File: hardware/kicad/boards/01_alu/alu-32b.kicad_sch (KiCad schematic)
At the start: 97 parts, among them J1 Conn_02x06_Odd_Even, J2 Conn_02x04_Odd_Even, J3 Conn_02x16_Counter_Clockwise, J4 Conn_02x16_Counter_Clockwise, J5 Conn_02x16_Counter_Clockwise, J6 Conn_02x16_Counter_Clockwise, SW1 SW_DIP_x08, SW10 SW_DIP_x08, SW11 SW_DIP_x08, SW12 SW_DIP_x08, SW13 SW_SPDT, SW2 SW_DIP_x08, SW3 SW_DIP_x08, SW4 SW_DIP_x08, SW5 SW_DIP_x08, SW6 SW_DIP_x08, SW7 SW_DIP_x08, SW8 SW_DIP_x08, SW9 SW_DIP_x08, U1 74HC86, U10 74LS30, U11 74LS182, U12 74LS182, U13 74LS182, U14 74LS30, U15 74LS182, U16 74LS182, U17 74LS182, U18 74LS182, U19 74LS182, U2 74LS153, U20 74LS182, U21 74LS182, U22 74LS182, U23 74LS540, U24 74LS377, U25 74LS377, U3 74AHC541, U4 74HCT00, U5 74AHCT1G08, U6 74AHC1G04, U7 74LS30, U8 74AHC541, U9 74LS30

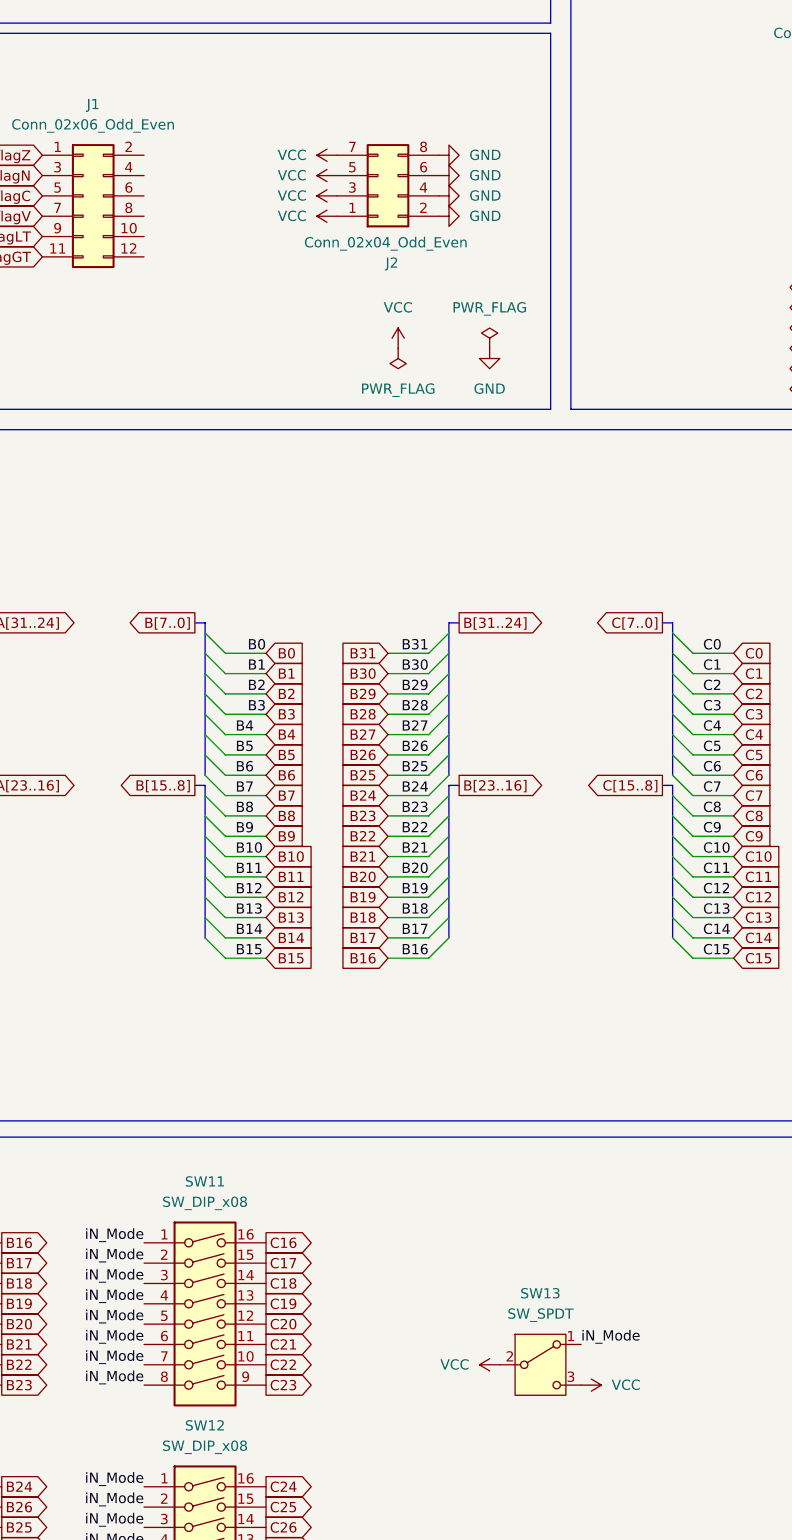
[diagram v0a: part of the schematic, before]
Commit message: chore: removed extra vcc on inMode switch; added missing flags export to pinSocket out pins
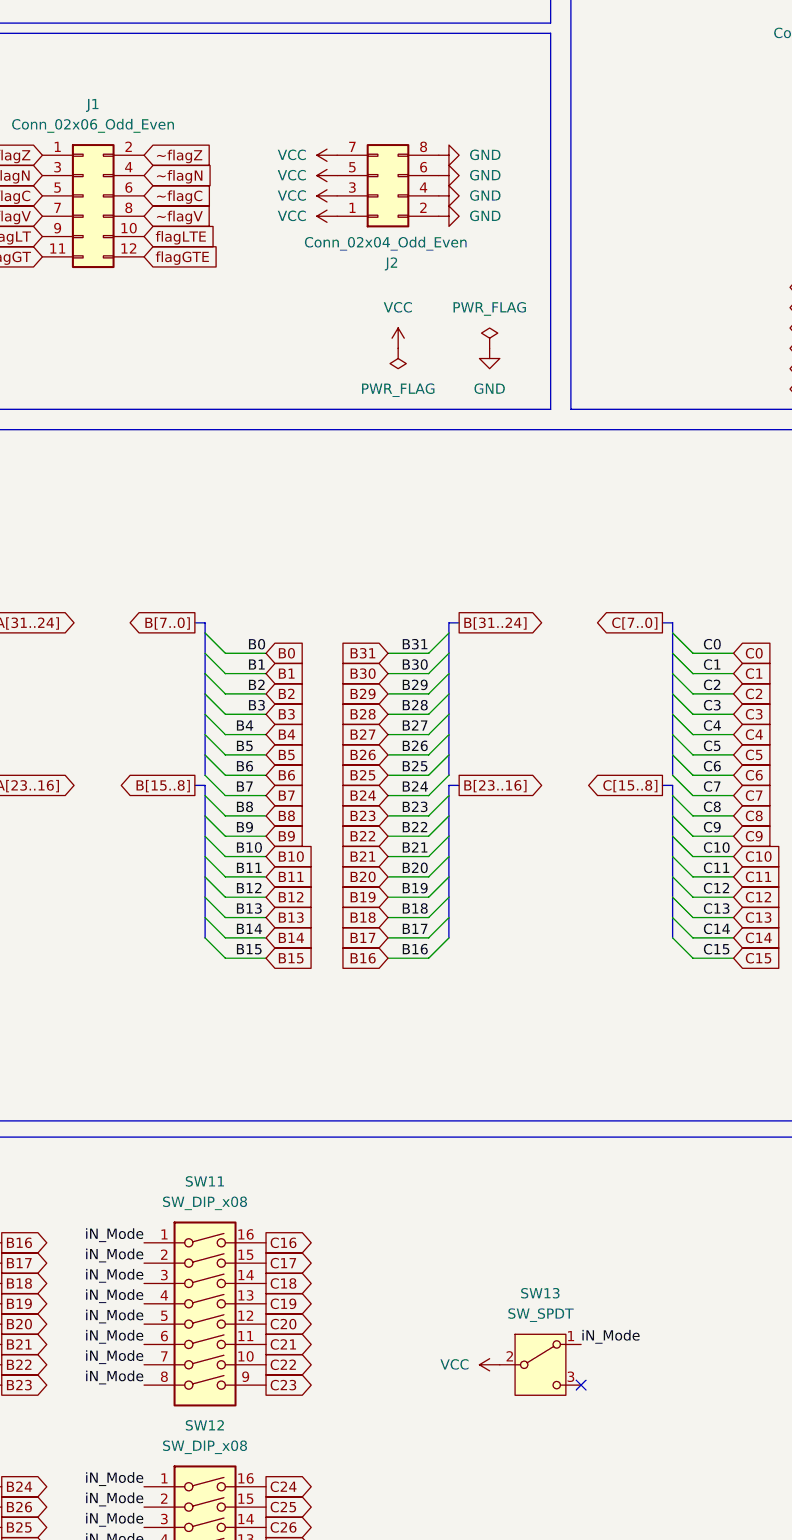
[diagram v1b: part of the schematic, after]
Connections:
- net VCC: no longer SW13.3 (C)
- net flagGTE: now also J1.12 (Pin_12)
- net flagLTE: now also J1.10 (Pin_10)
- net ~flagC: now also J1.6 (Pin_6)
- net ~flagN: now also J1.4 (Pin_4)
- net ~flagV: now also J1.8 (Pin_8)
- net ~flagZ: now also J1.2 (Pin_2)
- no-connect marks 25 -> 26
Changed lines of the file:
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@@
 	)
 	(no_connect
+		(at 273.05 495.3)
+	)
+	(no_connect
 		(at 35.56 251.46)
 	)
@@
 		)
 	)
+	(global_label "~flagC"
+		(shape input)
+		(at 218.44 346.71 0)
+		(fields_autoplaced yes)
+		(effects
+			(font
+				(size 1.27 1.27)
+			)
+			(justify left)
+		)
+		(property "Intersheetrefs" "${INTERSHEET_REFS}"
+			(at 227.2912 346.71 0)
+			(hide yes)
+			(show_name no)
+			(do_not_autoplace no)
+			(effects
+				(font
+					(size 1.27 1.27)
+				)
+				(justify left)
+			)
+		)
+	)
 	(global_label "B13"
 		(shape input)
@@
 		)
 	)
+	(global_label "~flagV"
+		(shape input)
+		(at 218.44 349.25 0)
+		(fields_autoplaced yes)
+		(effects
+			(font
+				(size 1.27 1.27)
+			)
+			(justify left)
+		)
+		(property "Intersheetrefs" "${INTERSHEET_REFS}"
+			(at 227.1098 349.25 0)
+			(hide yes)
+			(show_name no)
+			(do_not_autoplace no)
+			(effects
+				(font
+					(size 1.27 1.27)
+				)
+				(justify left)
+			)
+		)
+	)
 	(global_label "A12"
 		(shape output)
@@
 		)
 	)
+	(global_label "~flagN"
+		(shape input)
+		(at 218.44 344.17 0)
+		(fields_autoplaced yes)
+		(effects
+			(font
+				(size 1.27 1.27)
+			)
+			(justify left)
+		)
+		(property "Intersheetrefs" "${INTERSHEET_REFS}"
+			(at 227.3517 344.17 0)
+			(hide yes)
+			(show_name no)
+			(do_not_autoplace no)
+			(effects
+				(font
+					(size 1.27 1.27)
+				)
+				(justify left)
+			)
+		)
+	)
 	(global_label "flagWE"
 		(shape input)
@@
 		)
 	)
+	(global_label "flagLTE"
+		(shape input)
+		(at 218.44 351.79 0)
+		(fields_autoplaced yes)
+		(effects
+			(font
+				(size 1.27 1.27)
+			)
+			(justify left)
+		)
+		(property "Intersheetrefs" "${INTERSHEET_REFS}"
+			(at 228.2588 351.79 0)
+			(hide yes)
+			(show_name no)
+			(do_not_autoplace no)
+			(effects
+				(font
+					(size 1.27 1.27)
+				)
+				(justify left)
+			)
+		)
+	)
 	(global_label "A4"
 		(shape input)
@@
 		)
 	)
+	(global_label "flagGTE"
+		(shape input)
+		(at 218.44 354.33 0)
+		(fields_autoplaced yes)
+		(effects
+			(font
+				(size 1.27 1.27)
+			)
+			(justify left)
+		)
+		(property "Intersheetrefs" "${INTERSHEET_REFS}"
+			(at 228.5007 354.33 0)
+			(hide yes)
+			(show_name no)
+			(do_not_autoplace no)
+			(effects
+				(font
+					(size 1.27 1.27)
+				)
+				(justify left)
+			)
+		)
+	)
 	(global_label "CIN-SEL"
 		(shape input)
@@
 		)
 	)
+	(global_label "~flagZ"
+		(shape input)
+		(at 218.44 341.63 0)
+		(fields_autoplaced yes)
+		(effects
+			(font
+				(size 1.27 1.27)
+			)
+			(justify left)
+		)
+		(property "Intersheetrefs" "${INTERSHEET_REFS}"
+			(at 227.2307 341.63 0)
+			(hide yes)
+			(show_name no)
+			(do_not_autoplace no)
+			(effects
+				(font
+					(size 1.27 1.27)
+				)
+				(justify left)
+			)
+		)
+	)
 	(global_label "Ceff2"
 		(shape output)
@@
 					(unit 1)
 				)
-			)
-		)
-	)
-	(symbol
-		(lib_id "power:VCC")
-		(at 273.05 495.3 270)
-		(mirror x)
-		(unit 1)
-		(body_style 1)
-		(exclude_from_sim no)
-		(in_bom yes)
-		(on_board yes)
-		(in_pos_files yes)
-		(dnp no)
-		(property "Reference" "#PWR077"
-			(at 269.24 495.3 0)
-			(hide yes)
-			(show_name no)
-			(do_not_autoplace no)
-			(effects
-				(font
-					(size 1.27 1.27)
-				)
-			)
-		)
-		(property "Value" "VCC"
-			(at 276.86 495.2999 90)
-			(show_name no)
-			(do_not_autoplace no)
-			(effects
-				(font
-					(size 1.27 1.27)
-				)
-				(justify left)
-			)
-		)
-		(property "Footprint" ""
-			(at 273.05 495.3 0)
-			(hide yes)
-			(show_name no)
-			(do_not_autoplace no)
-			(effects
-				(font
-					(size 1.27 1.27)
-				)
-			)
-		)
-		(property "Datasheet" ""
-			(at 273.05 495.3 0)
-			(hide yes)
-			(show_name no)
-			(do_not_autoplace no)
-			(effects
-				(font
-					(size 1.27 1.27)
-				)
-			)
-		)
-		(property "Description" "Power symbol creates a global label with name \"VCC\""
-			(at 273.05 495.3 0)
-			(hide yes)
-			(show_name no)
-			(do_not_autoplace no)
-			(effects
-				(font
-					(size 1.27 1.27)
-				)
-			)
-		)
-		(pin "1"
-		)
-		(instances
-			(project "alu-32b"
-				(path "/ddad1417-0afc-402d-a021-92fc87ddd78a"
-					(reference "#PWR077")
-					(unit 1)
-				)

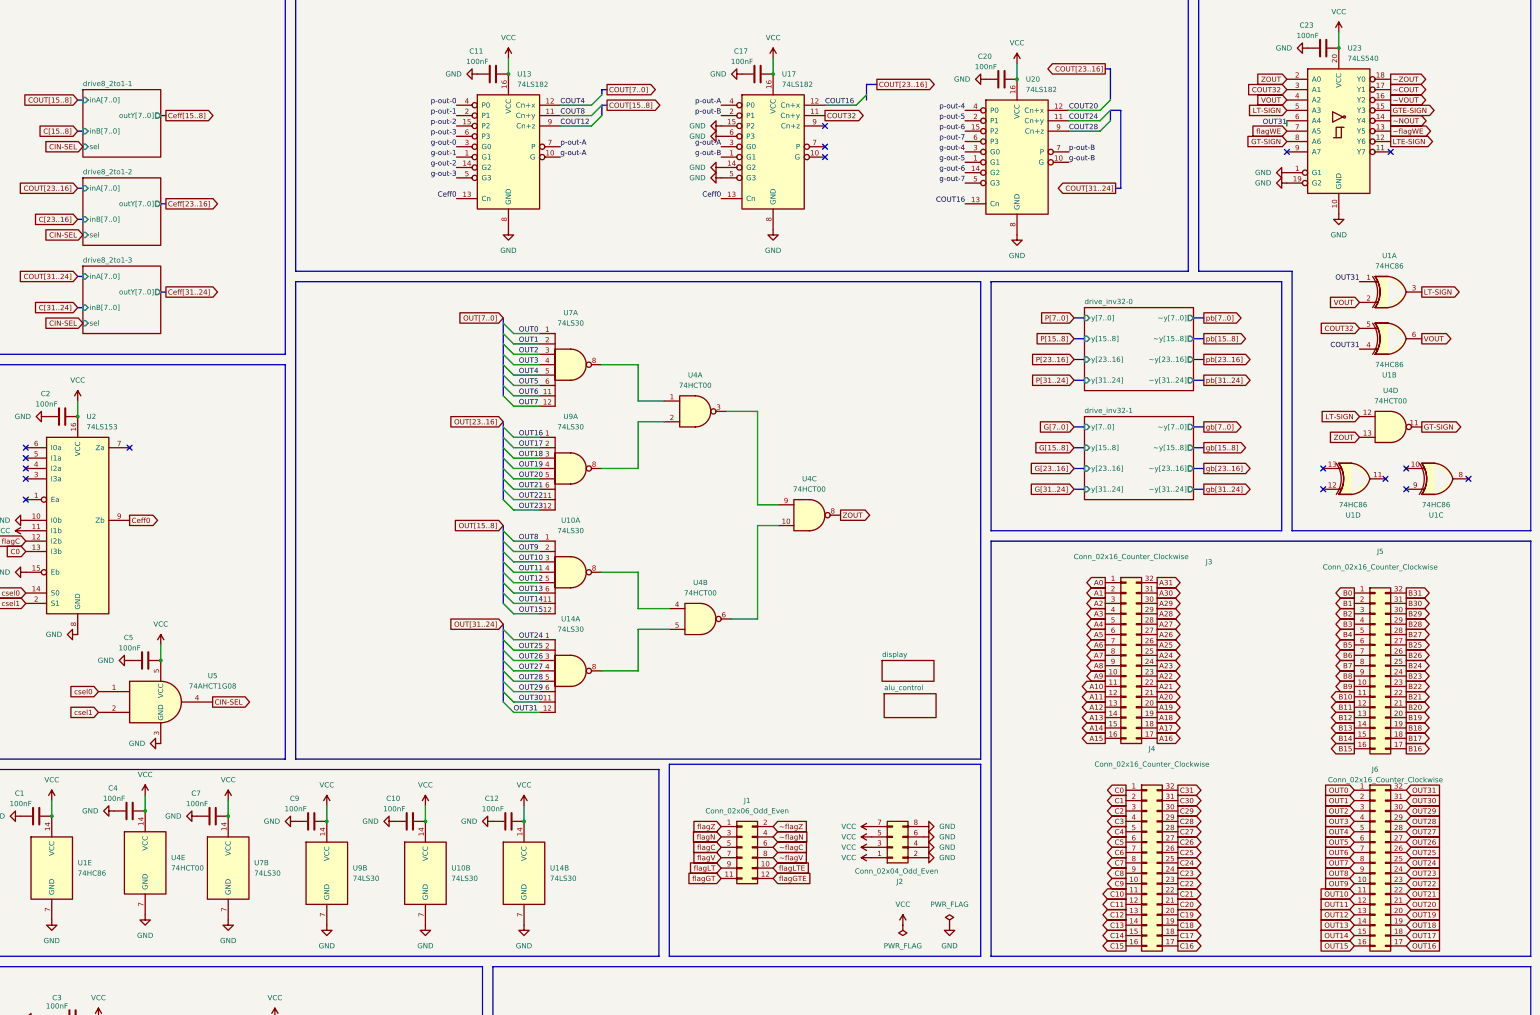
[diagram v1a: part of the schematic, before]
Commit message: fix: fixed the zero flag detection logic
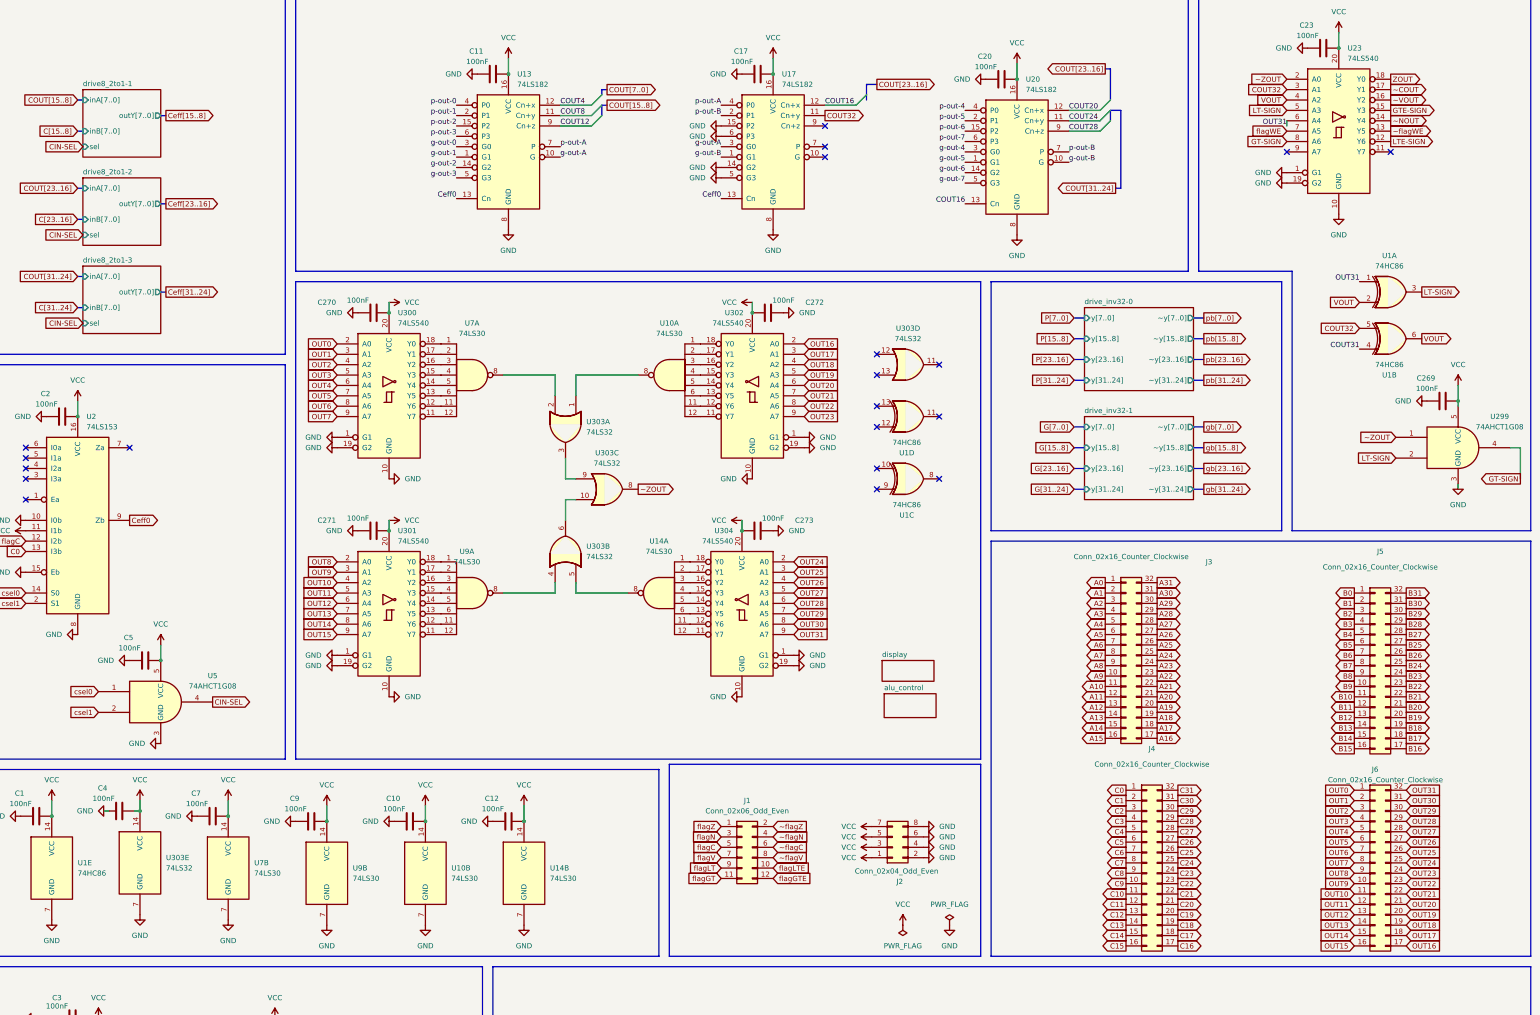
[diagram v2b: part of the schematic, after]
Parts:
- removed U4: 74HCT00, Package_SO:SOIC-14_3.9x8.7mm_P1.27mm, symbol 74xx:74HCT00
- added C269, C270, C271, C272, C273: 100nF, Capacitor_SMD:C_0805_2012Metric, symbol Device:C
- added U299: 74AHCT1G08, Package_TO_SOT_SMD:SOT-23-5, symbol 74xGxx:74AHCT1G08
- added U300, U301, U302, U304: 74LS540, Package_SO:SOIC-20W_7.5x12.8mm_P1.27mm, symbol 74xx:74LS540
- added U303: 74LS32, symbol 74xx:74LS32
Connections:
- net GND: now also C269.1, C270.1, C271.1, C272.1, C273.1, U299.3 (GND), U300.1 (G1), U300.10 (GND), U300.19 (G2), U301.1 (G1), U301.10 (GND), U301.19 (G2), U302.1 (G1), U302.10 (GND), U302.19 (G2), U303.7 (GND), U304.1 (G1), U304.10 (GND), U304.19 (G2)
- net GT-SIGN: now also U299.4
- net LT-SIGN: now also U299.2
- net OUT0: now also U300.2 (A0); no longer U7.1
- net OUT1: now also U300.3 (A1); no longer U7.2
- net OUT10: now also U301.4 (A2); no longer U10.3
- net OUT11: now also U301.5 (A3); no longer U10.4
- net OUT12: now also U301.6 (A4); no longer U10.5
- net OUT13: now also U301.7 (A5); no longer U10.6
- net OUT14: now also U301.8 (A6); no longer U10.11
- net OUT15: now also U301.9 (A7); no longer U10.12
- net OUT16: now also U302.2 (A0); no longer U9.1
- net OUT17: now also U302.3 (A1); no longer U9.2
- net OUT18: now also U302.4 (A2); no longer U9.3
- net OUT19: now also U302.5 (A3); no longer U9.4
- net OUT2: now also U300.4 (A2); no longer U7.3
- net OUT20: now also U302.6 (A4); no longer U9.5
- net OUT21: now also U302.7 (A5); no longer U9.6
- net OUT22: now also U302.8 (A6); no longer U9.11
- net OUT23: now also U302.9 (A7); no longer U9.12
- net OUT24: now also U304.2 (A0); no longer U14.1
- net OUT25: now also U304.3 (A1); no longer U14.2
- net OUT26: now also U304.4 (A2); no longer U14.3
- net OUT27: now also U304.5 (A3); no longer U14.4
- net OUT28: now also U304.6 (A4); no longer U14.5
- net OUT29: now also U304.7 (A5); no longer U14.6
- net OUT3: now also U300.5 (A3); no longer U7.4
- net OUT30: now also U304.8 (A6); no longer U14.11
- net OUT31: now also U304.9 (A7); no longer U14.12
- net OUT4: now also U300.6 (A4); no longer U7.5
- net OUT5: now also U300.7 (A5); no longer U7.6
- net OUT6: now also U300.8 (A6); no longer U7.11
- net OUT7: now also U300.9 (A7); no longer U7.12
- net OUT8: now also U301.2 (A0); no longer U10.1
- net OUT9: now also U301.3 (A1); no longer U10.2
- net VCC: now also C269.2, C270.2, C271.2, C272.2, C273.2, U299.5 (VCC), U300.20 (VCC), U301.20 (VCC), U302.20 (VCC), U303.14 (VCC), U304.20 (VCC)
- net ZOUT: now also U23.18 (Y0); no longer U23.2 (A0)
- net ~ZOUT: now also U23.2 (A0), U299.1, U303.8; no longer U23.18 (Y0)
- net at U7.8: now also U303.2
- net at U9.8: now also U303.4
- net at U10.8: now also U303.1
- net at U14.8: now also U303.5
- new net: U301.11 (Y7), U9.12
- new net: U301.12 (Y6), U9.11
- new net: U301.13 (Y5), U9.6
- new net: U301.14 (Y4), U9.5
- new net: U301.15 (Y3), U9.4
- new net: U301.16 (Y2), U9.3
- new net: U301.17 (Y1), U9.2
- new net: U301.18 (Y0), U9.1
- new net: U10.1, U302.18 (Y0)
- new net: U10.11, U302.12 (Y6)
- new net: U10.12, U302.11 (Y7)
- new net: U10.2, U302.17 (Y1)
- new net: U10.3, U302.16 (Y2)
- new net: U10.4, U302.15 (Y3)
- new net: U10.5, U302.14 (Y4)
- new net: U10.6, U302.13 (Y5)
- new net: U14.12, U304.11 (Y7)
- new net: U14.11, U304.12 (Y6)
- new net: U14.6, U304.13 (Y5)
- new net: U14.5, U304.14 (Y4)
- new net: U14.4, U304.15 (Y3)
- new net: U14.3, U304.16 (Y2)
- new net: U14.2, U304.17 (Y1)
- new net: U14.1, U304.18 (Y0)
- new net: U303.10, U303.6
- new net: U303.3, U303.9
- new net: U300.11 (Y7), U7.12
- new net: U300.12 (Y6), U7.11
- new net: U300.13 (Y5), U7.6
- new net: U300.14 (Y4), U7.5
- new net: U300.15 (Y3), U7.4
- new net: U300.16 (Y2), U7.3
- new net: U300.17 (Y1), U7.2
- new net: U300.18 (Y0), U7.1
- no-connect marks 26 -> 29
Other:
- title: (none) -> Tomato32 ALU
- moved on the sheet: C4, U10A, U14A, U1C, U1D, U7A, U9A
